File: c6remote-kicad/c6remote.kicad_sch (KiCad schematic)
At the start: 24 parts, among them J1 Battery, Q1 MMBT2222A, SW1 SW_Push, SW10 SW_Push, SW11 SW_Push, SW2 SW_Push, SW3 SW_Push, SW4 SW_Push, SW5 SW_Push, SW6 SW_Push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

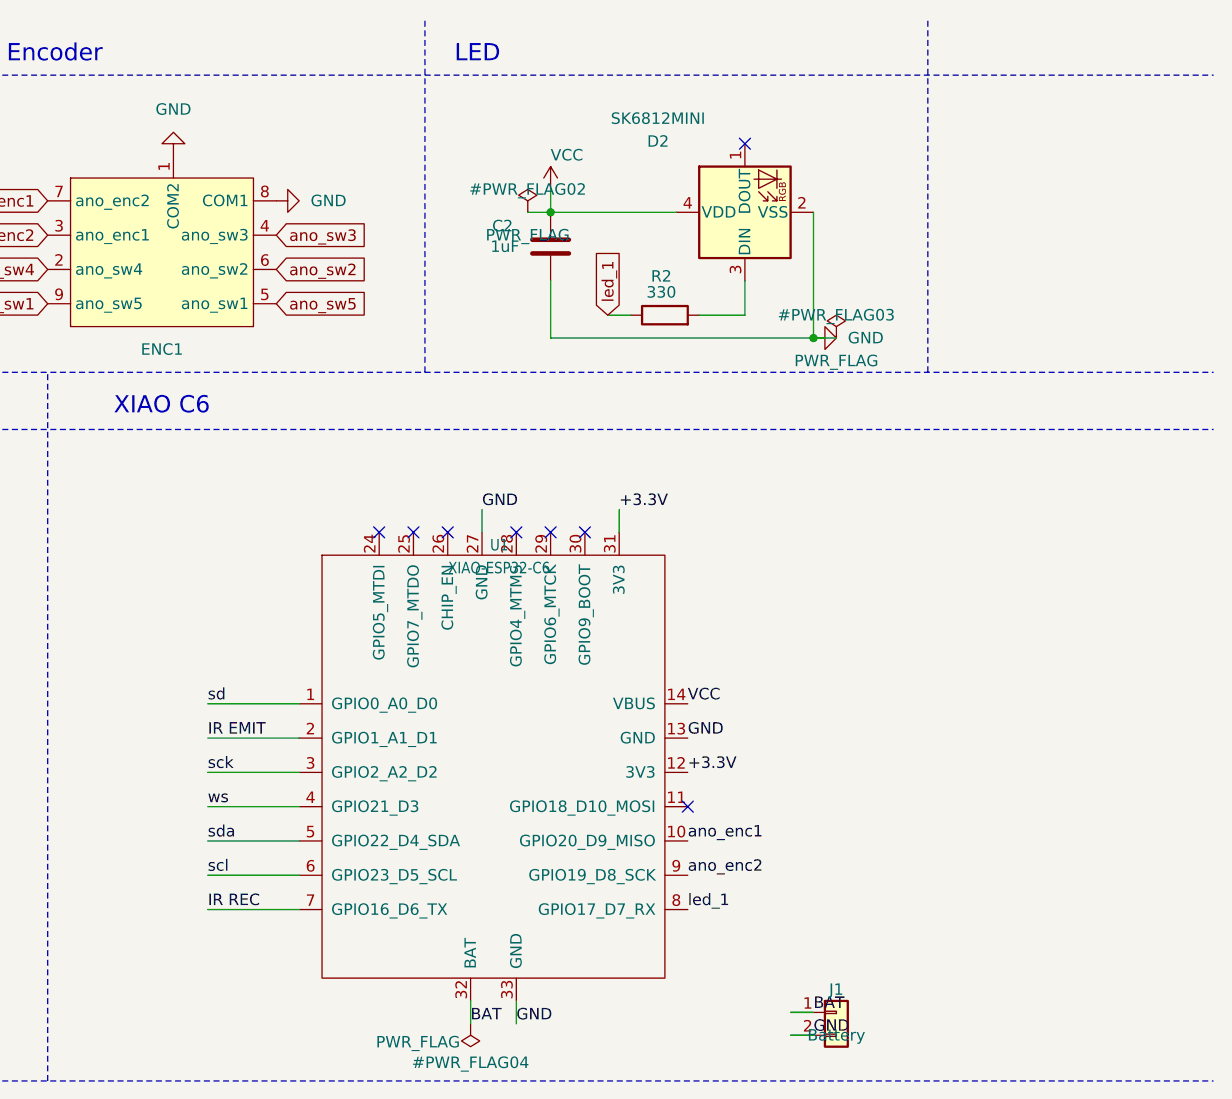
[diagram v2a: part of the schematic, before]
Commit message: feat(kicad): move battery connector layout
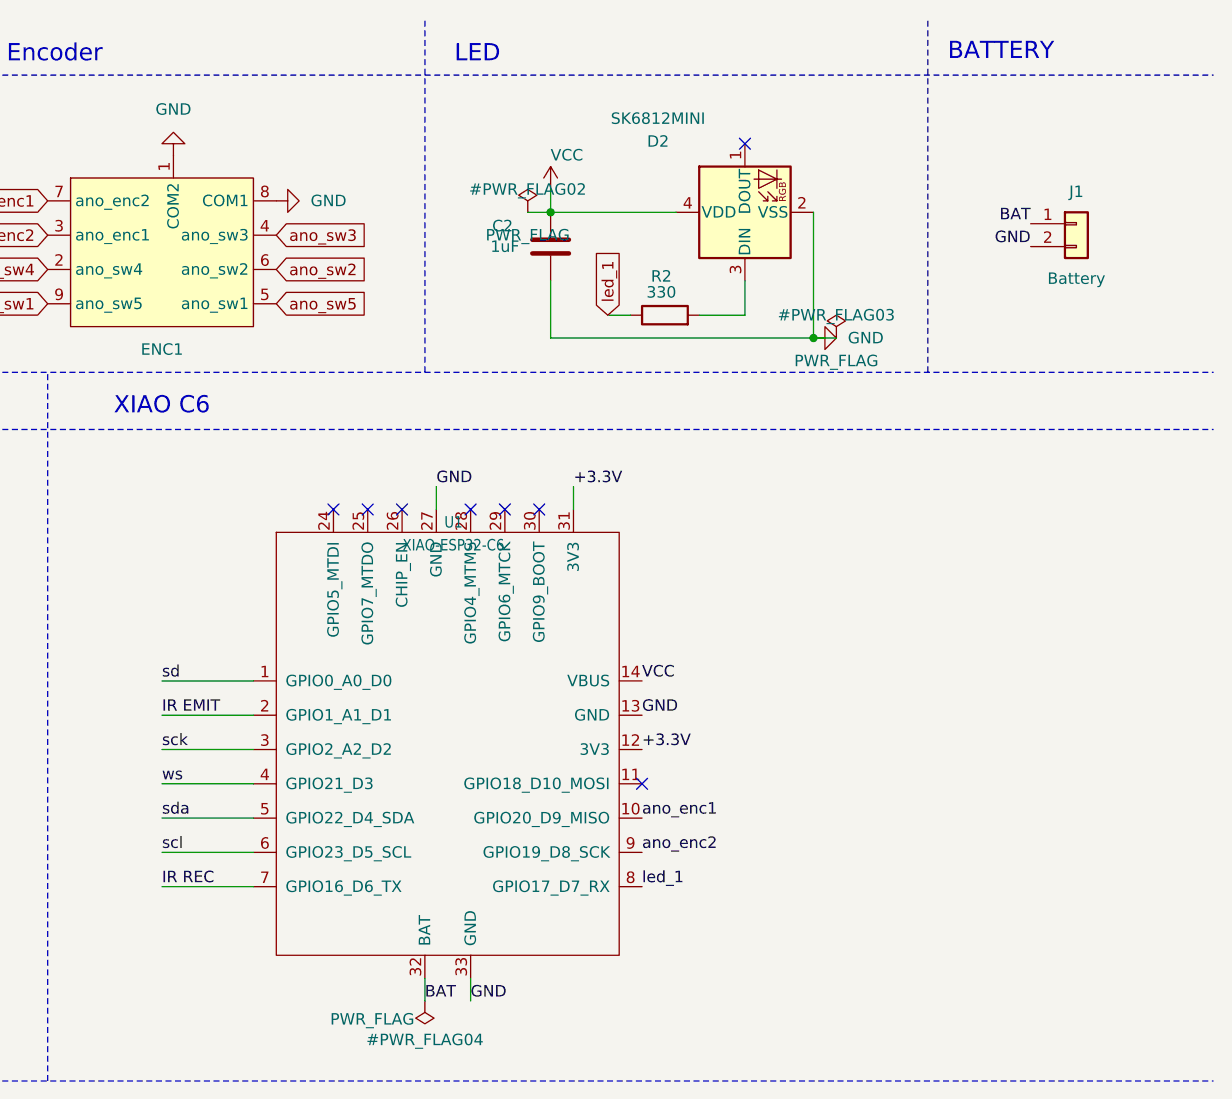
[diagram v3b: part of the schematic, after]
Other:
- note added: "BATTERY"
- moved on the sheet: J1, U1
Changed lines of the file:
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@@
 	(generator_version "10.0")
 	(paper "A4")
+	(text "BATTERY"
+		(exclude_from_sim no)
+		(at 262.128 15.24 0)
+		(effects
+			(font
+				(size 1.905 1.905)
+			)
+		)
+	)
 	(text "XIAO C6"
 		(exclude_from_sim no)
@@
 	)
 	(no_connect
-		(at 227.33 99.06)
+		(at 222.25 96.52)
 	)
 	(no_connect
-		(at 215.9 68.58)
+		(at 210.82 66.04)
 	)
 	(no_connect
-		(at 212.09 68.58)
+		(at 207.01 66.04)
 	)
 	(no_connect
@@
 	)
 	(no_connect
-		(at 200.66 68.58)
+		(at 195.58 66.04)
 	)
 	(no_connect
-		(at 208.28 68.58)
+		(at 203.2 66.04)
 	)
 	(no_connect
-		(at 193.04 68.58)
+		(at 187.96 66.04)
 	)
 	(no_connect
@@
 	)
 	(no_connect
-		(at 196.85 68.58)
+		(at 191.77 66.04)
 	)
 	(wire
@@
 	(wire
 		(pts
-			(xy 173.99 95.25) (xy 184.15 95.25)
+			(xy 168.91 92.71) (xy 179.07 92.71)
 		)
 		(stroke
@@
 	(wire
 		(pts
-			(xy 173.99 99.06) (xy 184.15 99.06)
+			(xy 168.91 96.52) (xy 179.07 96.52)
 		)
 		(stroke
@@
 	(wire
 		(pts
-			(xy 173.99 106.68) (xy 184.15 106.68)
+			(xy 168.91 104.14) (xy 179.07 104.14)
 		)
 		(stroke
@@
 	(wire
 		(pts
-			(xy 219.71 68.58) (xy 219.71 66.04)
+			(xy 214.63 66.04) (xy 214.63 63.5)
 		)
 		(stroke
@@
 	(wire
 		(pts
-			(xy 204.47 68.58) (xy 204.47 66.04)
+			(xy 199.39 66.04) (xy 199.39 63.5)
 		)
 		(stroke
@@
 	(wire
 		(pts
-			(xy 173.99 102.87) (xy 184.15 102.87)
+			(xy 168.91 100.33) (xy 179.07 100.33)
 		)
 		(stroke
@@
 	(wire
 		(pts
-			(xy 173.99 110.49) (xy 184.15 110.49)
+			(xy 168.91 107.95) (xy 179.07 107.95)
 		)
 		(stroke
@@
 	(wire
 		(pts
-			(xy 238.76 124.46) (xy 241.3 124.46)
-		)
-		(stroke
-			(width 0)
-			(type default)
-		)
-	)
-	(wire
-		(pts
-			(xy 203.2 123.19) (xy 203.2 120.65)
-		)
-		(stroke
-			(width 0)
-			(type default)
-		)
-	)
-	(wire
-		(pts
-			(xy 238.76 121.92) (xy 241.3 121.92)
+			(xy 198.12 120.65) (xy 198.12 118.11)
 		)
 		(stroke
@@
 	(wire
 		(pts
-			(xy 173.99 91.44) (xy 184.15 91.44)
+			(xy 168.91 88.9) (xy 179.07 88.9)
 		)
 		(stroke
@@
 	(wire
 		(pts
-			(xy 173.99 87.63) (xy 184.15 87.63)
+			(xy 168.91 85.09) (xy 179.07 85.09)
 		)
 		(stroke
@@
 	(wire
 		(pts
-			(xy 208.28 120.65) (xy 208.28 123.19)
+			(xy 203.2 118.11) (xy 203.2 120.65)
 		)
 		(stroke
@@
 	)
 	(label "ano_enc2"
-		(at 227.33 106.68 0)
+		(at 222.25 104.14 0)
 		(effects
 			(font
@@
 	)
 	(label "GND"
-		(at 204.47 66.04 0)
+		(at 199.39 63.5 0)
 		(effects
 			(font
@@
 	)
 	(label "VCC"
-		(at 227.33 87.63 0)
+		(at 222.25 85.09 0)
 		(effects
 			(font
@@
 	)
 	(label "IR REC"
-		(at 173.99 110.49 0)
+		(at 168.91 107.95 0)
 		(effects
 			(font
@@
 	)
 	(label "GND"
-		(at 241.3 124.46 0)
+		(at 265.43 36.83 180)
 		(effects
 			(font
 				(size 1.27 1.27)
 			)
-			(justify left bottom)
+			(justify right bottom)
 		)
 	)
 	(label "+3.3V"
-		(at 219.71 66.04 0)
+		(at 214.63 63.5 0)
 		(effects
 			(font
@@
 	)
 	(label "GND"
-		(at 227.33 91.44 0)
+		(at 222.25 88.9 0)
 		(effects
 			(font
@@
 	)
 	(label "sck"
-		(at 173.99 95.25 0)
+		(at 168.91 92.71 0)
 		(effects
 			(font
@@
 	)
 	(label "ano_enc1"
-		(at 227.33 102.87 0)
+		(at 222.25 100.33 0)
 		(effects
 			(font
@@
 	)
 	(label "sda"
-		(at 173.99 102.87 0)
+		(at 168.91 100.33 0)
 		(effects
 			(font
@@
 	)
 	(label "sd"
-		(at 173.99 87.63 0)
+		(at 168.91 85.09 0)
 		(effects
 			(font
@@
 	)
 	(label "BAT"
-		(at 241.3 121.92 0)
+		(at 265.43 34.29 180)
 		(effects
 			(font
 				(size 1.27 1.27)
 			)
-			(justify left bottom)
+			(justify right bottom)
 		)
 	)
 	(label "+3.3V"
-		(at 227.33 95.25 0)
+		(at 222.25 92.71 0)
 		(effects
 			(font
@@
 	)
 	(label "led_1"
-		(at 227.33 110.49 0)
+		(at 222.25 107.95 0)
 		(effects
 			(font
@@
 	)
 	(label "GND"
-		(at 208.28 123.19 0)
+		(at 203.2 120.65 0)
 		(effects
 			(font
@@
 	)
 	(label "ws"
-		(at 173.99 99.06 0)
+		(at 168.91 96.52 0)
 		(effects
 			(font
@@
 	)
 	(label "scl"
-		(at 173.99 106.68 0)
+		(at 168.91 104.14 0)
 		(effects
 			(font
@@
 	)
 	(label "BAT"
-		(at 203.2 123.19 0)
+		(at 198.12 120.65 0)
 		(effects
 			(font
@@
 	)
 	(label "IR EMIT"
-		(at 173.99 91.44 0)
+		(at 168.91 88.9 0)
 		(effects
 			(font
@@
 	(symbol
 		(lib_id "Seeed_Studio_XIAO_Series:XIAO-ESP32-C6-SMD")
-		(at 205.74 91.44 0)
+		(at 200.66 88.9 0)
 		(unit 1)
 		(body_style 1)
@@
 		(dnp no)
 		(property "Reference" "U1"
-			(at 206.375 70 0)
+			(at 201.295 67.46 0)
 			(show_name no)
 			(do_not_autoplace no)
@@
 		)
 		(property "Value" "XIAO-ESP32-C6"
-			(at 206.375 72.54 0)
+			(at 201.295 70 0)
 			(show_name no)
 			(do_not_autoplace no)
@@
 		)
 		(property "Footprint" "Seeed_Studio_XIAO_Series:XIAO-ESP32-C6-SMD"
-			(at 201.168 109.982 0)
+			(at 196.088 107.442 0)
 			(hide yes)
 			(show_name no)
@@
 		)
 		(property "Datasheet" ""
-			(at 205.74 91.44 0)
+			(at 200.66 88.9 0)
 			(hide yes)
 			(show_name no)
@@
 		)
 		(property "Description" ""
-			(at 205.74 91.44 0)
+			(at 200.66 88.9 0)
 			(hide yes)
 			(show_name no)
@@
 		)
 		(property "Manufacturer" ""
-			(at 205.74 91.44 0)
+			(at 200.66 88.9 0)
 			(hide yes)
 			(show_name no)
@@
 		)
 		(property "MPN" ""
-			(at 205.74 91.44 0)
+			(at 200.66 88.9 0)
 			(hide yes)
 			(show_name no)
@@
 		)
 		(property "SKU" "XIAO-DIP"
-			(at 199.898 93.726 0)
+			(at 194.818 91.186 0)
 			(hide yes)
 			(show_name no)
@@
 		)
 		(property "Part Type" ""
-			(at 205.74 91.44 0)
+			(at 200.66 88.9 0)
 			(hide yes)
 			(show_name no)
@@
 		)
 		(property "Rating" ""
-			(at 205.74 91.44 0)
+			(at 200.66 88.9 0)
 			(show_name no)
 			(do_not_autoplace no)
@@
 		)
 		(property "Status" ""
-			(at 205.74 91.44 0)
+			(at 200.66 88.9 0)
 			(hide yes)
 			(show_name no)
@@
 		)
 		(property "Temperature" ""
-			(at 205.74 91.44 0)
+			(at 200.66 88.9 0)
 			(hide yes)
 			(show_name no)
@@
 		)
 		(property "Priority" ""
-			(at 205.74 91.44 0)
+			(at 200.66 88.9 0)
 			(hide yes)
 			(show_name no)
@@
 	(symbol
 		(lib_id "Connector_Generic:Conn_01x02")
-		(at 243.84 121.92 0)
+		(at 270.51 34.29 0)
 		(unit 1)
 		(body_style 1)
@@
 		(dnp no)
 		(property "Reference" "J1"
-			(at 243.84 119.38 0)
+			(at 270.51 30.734 0)
 			(show_name no)
 			(do_not_autoplace no)
@@
 		)
 		(property "Value" "Battery"
-			(at 243.84 124.46 0)
+			(at 270.51 40.386 0)
 			(show_name no)
 			(do_not_autoplace no)
@@
 		)
 		(property "Footprint" "Local:WirePad_1x02_P2.54mm_Back"
-			(at 243.84 121.92 0)
+			(at 270.51 34.29 0)
 			(hide yes)
 			(show_name no)
@@
 		)
 		(property "Datasheet" "~"
-			(at 243.84 121.92 0)
+			(at 270.51 34.29 0)
 			(hide yes)
 			(show_name no)
@@
 		)
 		(property "Description" ""
-			(at 243.84 121.92 0)
+			(at 270.51 34.29 0)
 			(show_name no)
 			(do_not_autoplace no)
@@
 	(symbol
 		(lib_id "power:PWR_FLAG")
-		(at 203.2 123.19 180)
+		(at 198.12 120.65 180)
 		(unit 1)
 		(body_style 1)
@@
 		(dnp no)
 		(property "Reference" "#PWR_FLAG04"
-			(at 203.2 127.508 0)
+			(at 198.12 124.968 0)
 			(show_name no)
 			(do_not_autoplace no)
@@
 		)
 		(property "Value" "PWR_FLAG"
-			(at 197.358 125.222 0)
+			(at 192.278 122.682 0)
 			(show_name no)
 			(do_not_autoplace no)
@@
 		)
 		(property "Footprint" ""
-			(at 203.2 123.19 0)
+			(at 198.12 120.65 0)
 			(hide yes)
 			(show_name no)
@@
 		)
 		(property "Datasheet" "~"
-			(at 203.2 123.19 0)
+			(at 198.12 120.65 0)
 			(hide yes)
 			(show_name no)
@@
 		)
 		(property "Description" ""
-			(at 203.2 123.19 0)
+			(at 198.12 120.65 0)
 			(show_name no)
 			(do_not_autoplace no)

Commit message: fix(kicad): update j1 footprint and todo
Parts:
- J1: footprint Local:WirePad_1x02_P2.54mm_Back -> Connector_JST:JST_PH_S2B-PH-K_1x02_P2.00mm_Horizontal
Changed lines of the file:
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@@
 			)
 		)
-		(property "Footprint" "Local:WirePad_1x02_P2.54mm_Back"
+		(property "Footprint" "Connector_JST:JST_PH_S2B-PH-K_1x02_P2.00mm_Horizontal"
 			(at 270.51 34.29 0)
 			(hide yes)

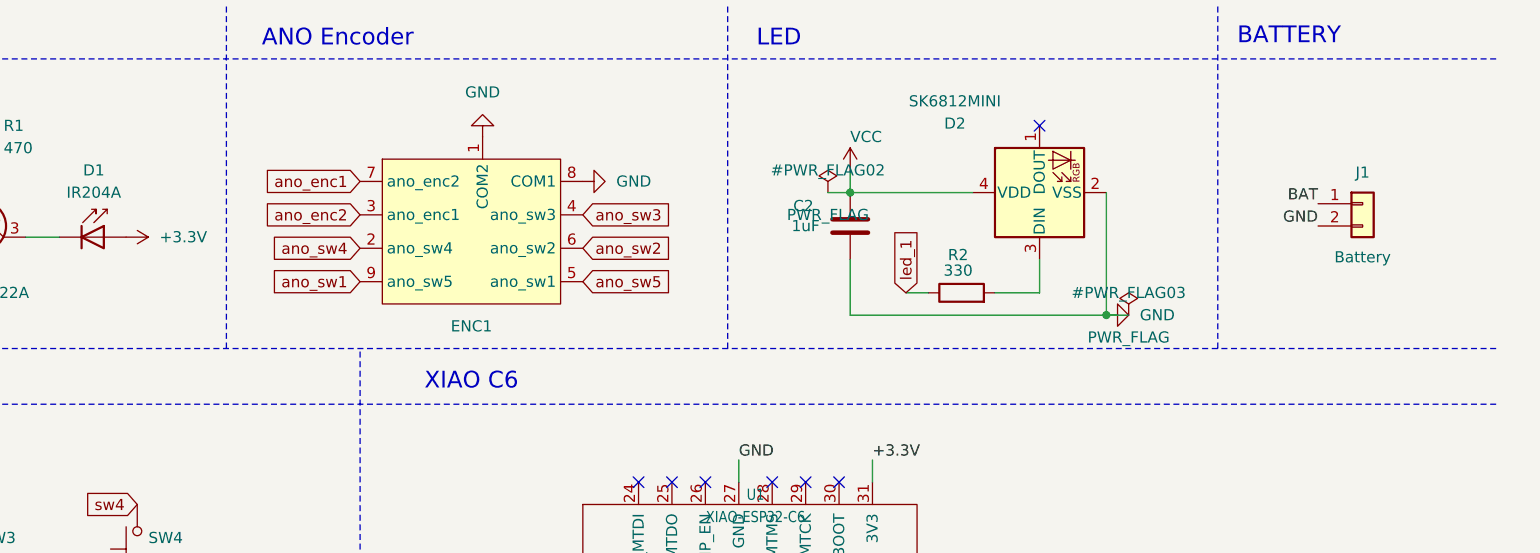
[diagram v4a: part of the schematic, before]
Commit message: docs(bom): add sourcing links and export
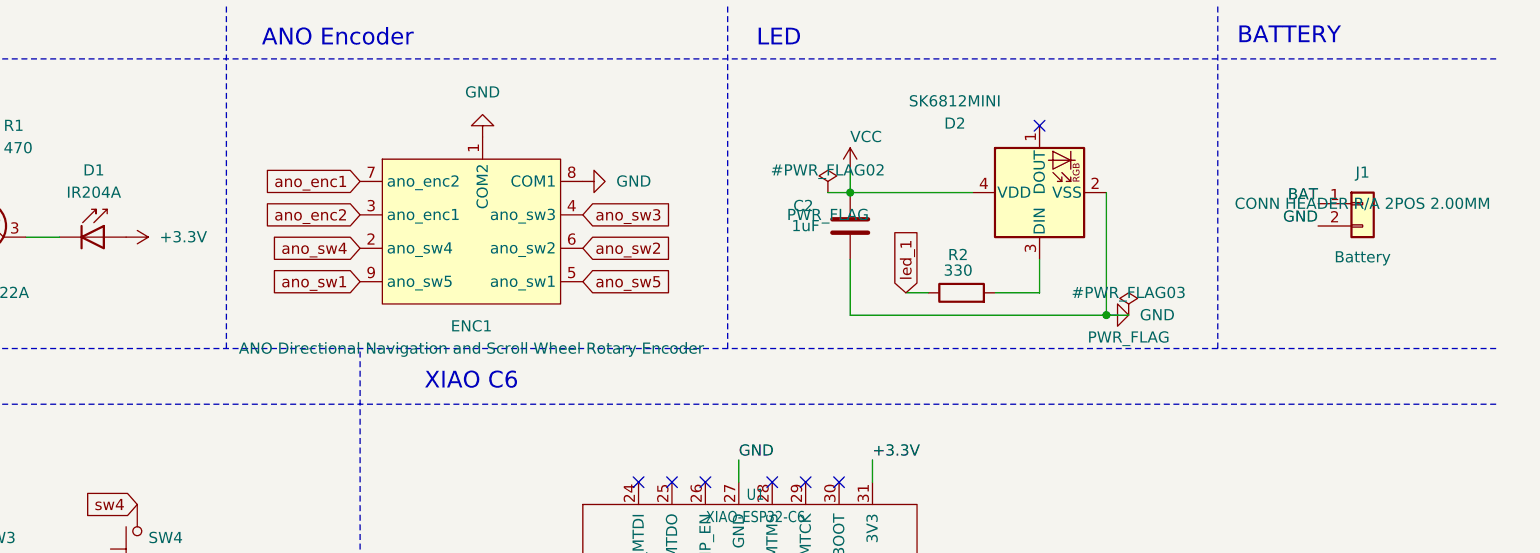
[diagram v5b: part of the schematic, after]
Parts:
- C1, C2: MPN (none) -> GRM21BR71A105MA01L; Manufacturer (none) -> Murata Electronics; SKU (none) -> 490-GRM21BR71A105MA01LCT-ND
- D1: MPN (none) -> IR204-A; Manufacturer (none) -> Everlight Electronics Co Ltd; SKU (none) -> 1080-1075-ND
- D2: MPN (none) -> 2686; Manufacturer (none) -> Adafruit Industries LLC; SKU (none) -> 1528-1541-ND
- ENC1: value (none) -> ANO Directional Navigation and Scroll Wheel Rotary Encoder; MPN (none) -> 5001; Manufacturer (none) -> Adafruit; SKU (none) -> 5001
- J1: MPN (none) -> S2B-PH-K-S(LF)(SN); Manufacturer (none) -> JST Sales America Inc.; SKU (none) -> 455-1719-ND
- MK1: MPN (none) -> ICS-43434; Manufacturer (none) -> TDK InvenSense; SKU (none) -> 1428-1066-1-ND
- Q1: MPN (none) -> MMBT2222A,215; Manufacturer (none) -> Nexperia USA Inc.; SKU (none) -> 1727-4043-1-ND
- R1: MPN (none) -> RC0603FR-07470RL; Manufacturer (none) -> YAGEO; SKU (none) -> 311-470HRCT-ND
- R2: MPN (none) -> RC0603FR-07330RL; Manufacturer (none) -> YAGEO; SKU (none) -> 311-330HRCT-ND
- SW1, SW10, SW11, SW2, SW3, SW4, SW5, SW6, SW7, SW8, SW9: MPN (none) -> TL3315NF160Q; Manufacturer (none) -> E-Switch; SKU (none) -> EG4621CT-ND
- U1: MPN (none) -> 113991254; Manufacturer (none) -> Seeed Technology Co., Ltd; SKU XIAO-DIP -> 1597-113991254-ND
- U2: MPN (none) -> TSOP4536; Manufacturer (none) -> Vishay Semiconductor Opto Division; SKU (none) -> TSOP4536-ND
- U3: MPN (none) -> PCF8575DBR; Manufacturer (none) -> Texas Instruments; SKU (none) -> 296-17856-1-ND

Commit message: chore(assets): regenerate readme previews
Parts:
- C1, C2: MPN GRM21BR71A105MA01L -> (none); Manufacturer Murata Electronics -> (none); SKU 490-GRM21BR71A105MA01LCT-ND -> (none)
- D1: MPN IR204-A -> (none); Manufacturer Everlight Electronics Co Ltd -> (none); SKU 1080-1075-ND -> (none)
- D2: MPN 2686 -> (none); Manufacturer Adafruit Industries LLC -> (none); SKU 1528-1541-ND -> (none)
- ENC1: value ANO Directional Navigation and Scroll Wheel Rotary Encoder -> (none); MPN 5001 -> (none); Manufacturer Adafruit -> (none); SKU 5001 -> (none)
- J1: MPN S2B-PH-K-S(LF)(SN) -> (none); Manufacturer JST Sales America Inc. -> (none); SKU 455-1719-ND -> (none)
- MK1: MPN ICS-43434 -> (none); Manufacturer TDK InvenSense -> (none); SKU 1428-1066-1-ND -> (none)
- Q1: MPN MMBT2222A,215 -> (none); Manufacturer Nexperia USA Inc. -> (none); SKU 1727-4043-1-ND -> (none)
- R1: MPN RC0603FR-07470RL -> (none); Manufacturer YAGEO -> (none); SKU 311-470HRCT-ND -> (none)
- R2: MPN RC0603FR-07330RL -> (none); Manufacturer YAGEO -> (none); SKU 311-330HRCT-ND -> (none)
- SW1, SW10, SW11, SW2, SW3, SW4, SW5, SW6, SW7, SW8, SW9: MPN TL3315NF160Q -> (none); Manufacturer E-Switch -> (none); SKU EG4621CT-ND -> (none)
- U1: MPN 113991254 -> (none); Manufacturer Seeed Technology Co., Ltd -> (none); SKU 1597-113991254-ND -> XIAO-DIP
- U2: MPN TSOP4536 -> (none); Manufacturer Vishay Semiconductor Opto Division -> (none); SKU TSOP4536-ND -> (none)
- U3: MPN PCF8575DBR -> (none); Manufacturer Texas Instruments -> (none); SKU 296-17856-1-ND -> (none)
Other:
- moved on the sheet: C2, D1, D2, ENC1, J1, MK1, Q1, R1, R2, U2

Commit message: docs(readme): add links and schematic frame
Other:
- note added: "homeThing C6"
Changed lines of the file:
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@@
+		)
+	)
+	(text "homeThing C6"
+		(exclude_from_sim no)
+		(at 201.168 174.752 0)
+		(effects
+			(font
+				(size 3.81 3.81)
+			)
 		)
 	)
